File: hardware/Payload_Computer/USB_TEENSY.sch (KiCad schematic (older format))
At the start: 7 parts, among them J2 USB_B_Micro

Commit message: More Library Updates
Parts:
- J2: symbol Payload_Computer-rescue:USB_B_Micro-Symbols -> Symbols:USB_B_Micro
- U?: symbol Payload_Computer-rescue:MKL02Z32VFG4-Symbols -> Symbols:MKL02Z32VFG4
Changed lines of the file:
@@
 $EndDescr
 $Comp
-L Payload_Computer-rescue:USB_B_Micro-Symbols J2
+L Symbols:USB_B_Micro J2
 U 1 1 5F87457D
 P 3150 3500
@@
 ID
 $Comp
-L Payload_Computer-rescue:MKL02Z32VFG4-Symbols U?
+L Symbols:MKL02Z32VFG4 U?
 U 1 1 5FB00371
 P 8350 3200

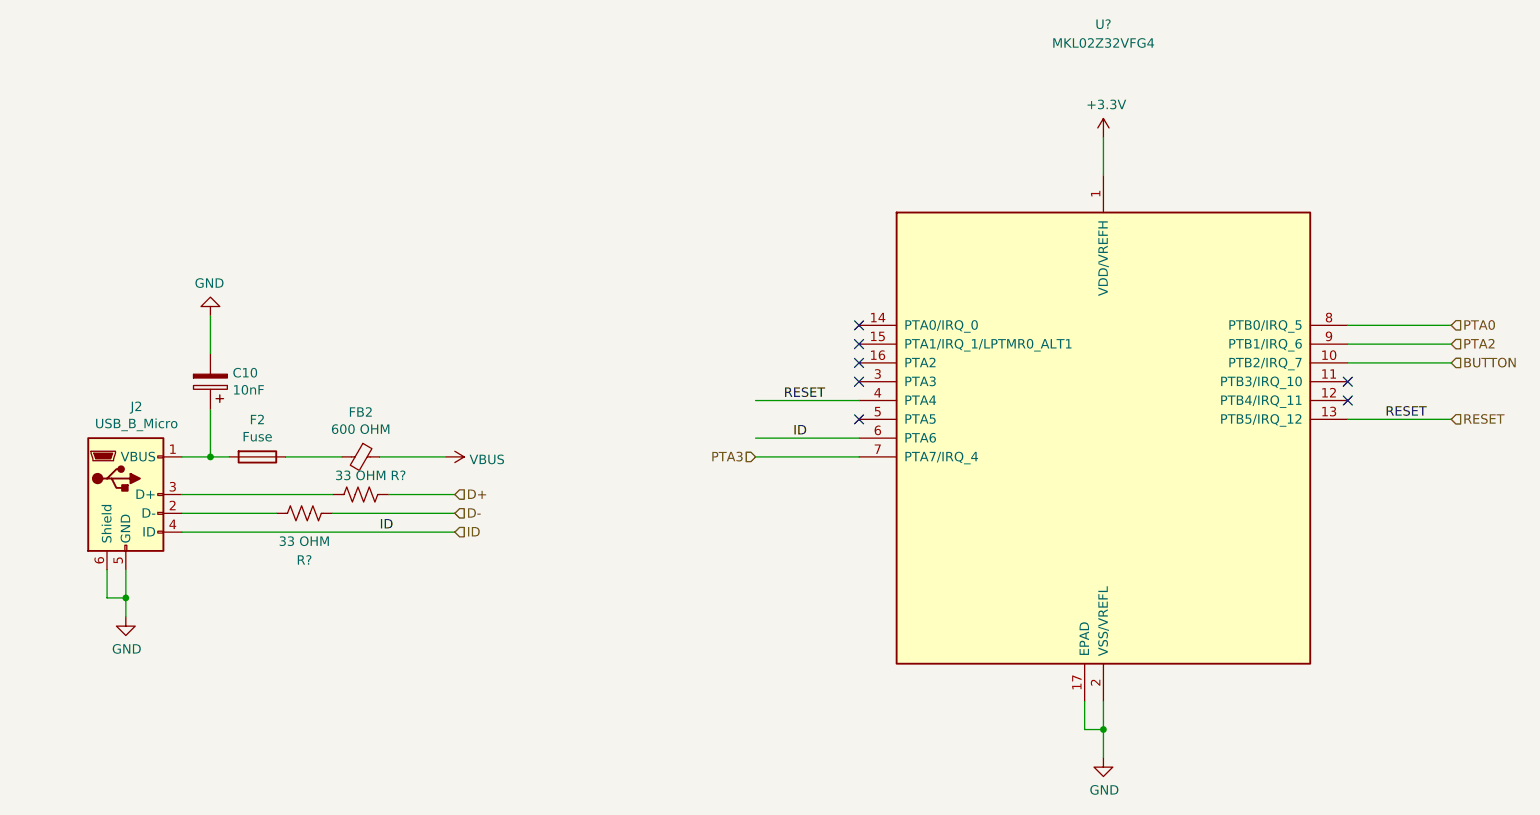
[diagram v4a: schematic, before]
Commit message: Finished Fan Schematic. Working on Servos
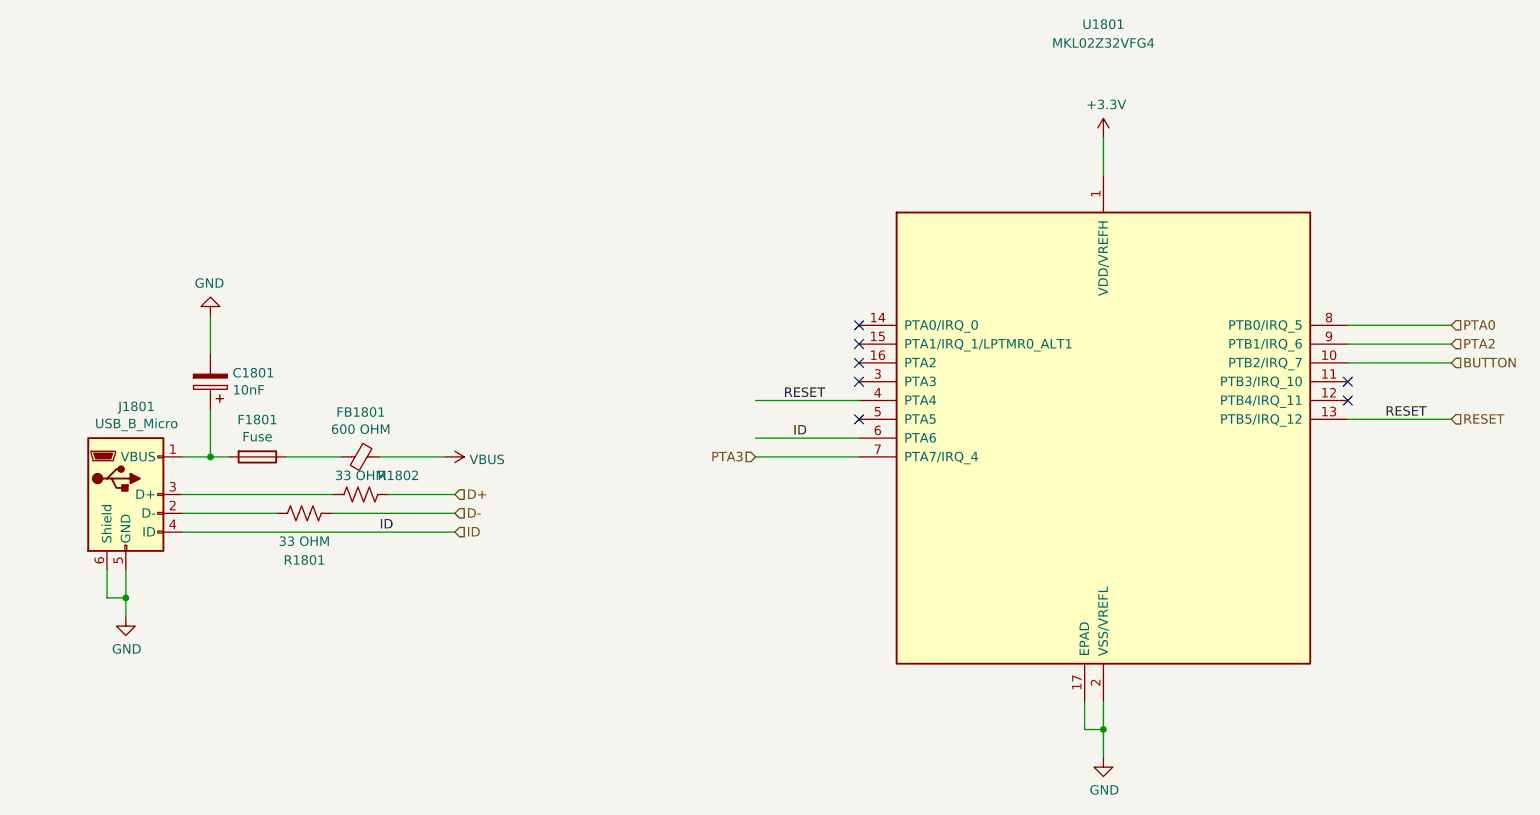
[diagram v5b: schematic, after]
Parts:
- C10: footprint (none) -> Capacitor_SMD:C_0603_1608Metric_Pad1.08x0.95mm_HandSolder
- R801, R802: renamed from R?; footprint (none) -> Resistor_SMD:R_0603_1608Metric_Pad0.98x0.95mm_HandSolder
- gave numbers to parts that had none: 1
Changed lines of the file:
@@
 $Descr A4 11693 8268
 encoding utf-8
-Sheet 8 26
+Sheet 18 22
 Title ""
 Date ""
@@
 P 3150 3500
 AR Path="/5F86D5A7/5F87457D" Ref="J2"  Part="1"
-AR Path="/60289E3E/5F87457D" Ref="J?"  Part="1"
-F 0 "J2" H 3207 3967 50  0000 C CNN
+AR Path="/60289E3E/5F87457D" Ref="J1801"  Part="1"
+F 0 "J1801" H 3207 3967 50  0000 C CNN
 F 1 "USB_B_Micro" H 3207 3876 50  0000 C CNN
 F 2 "" H 3300 3450 50  0001 C CNN
@@
 P 3850 3300
 AR Path="/5F86D5A7/5F874583" Ref="F2"  Part="1"
-AR Path="/60289E3E/5F874583" Ref="F?"  Part="1"
-F 0 "F2" V 3653 3300 50  0000 C CNN
+AR Path="/60289E3E/5F874583" Ref="F1801"  Part="1"
+F 0 "F1801" V 3653 3300 50  0000 C CNN
 F 1 "Fuse" V 3744 3300 50  0000 C CNN
 F 2 "" V 3780 3300 50  0001 C CNN
@@
 P 3600 2900
 AR Path="/5F86D5A7/5F87458A" Ref="C10"  Part="1"
-AR Path="/60289E3E/5F87458A" Ref="C?"  Part="1"
-F 0 "C10" H 3482 2854 50  0000 R CNN
+AR Path="/60289E3E/5F87458A" Ref="C1801"  Part="1"
+F 0 "C1801" H 3482 2854 50  0000 R CNN
 F 1 "10nF" H 3482 2945 50  0000 R CNN
-F 2 "" H 3638 2750 50  0001 C CNN
+F 2 "Capacitor_SMD:C_0603_1608Metric_Pad1.08x0.95mm_HandSolder" H 3638 2750 50  0001 C CNN
 F 3 "~" H 3600 2900 50  0001 C CNN
 	1    3600 2900
@@
 P 3600 2550
 AR Path="/5F86D5A7/5F874593" Ref="#PWR0117"  Part="1"
-AR Path="/60289E3E/5F874593" Ref="#PWR?"  Part="1"
-F 0 "#PWR0117" H 3600 2300 50  0001 C CNN
+AR Path="/60289E3E/5F874593" Ref="#PWR01802"  Part="1"
+F 0 "#PWR01802" H 3600 2300 50  0001 C CNN
 F 1 "GND" H 3605 2377 50  0000 C CNN
 F 2 "" H 3600 2550 50  0001 C CNN
@@
 P 4400 3300
 AR Path="/5F86D5A7/5F87459A" Ref="FB2"  Part="1"
-AR Path="/60289E3E/5F87459A" Ref="FB?"  Part="1"
-F 0 "FB2" V 4163 3300 50  0000 C CNN
+AR Path="/60289E3E/5F87459A" Ref="FB1801"  Part="1"
+F 0 "FB1801" V 4163 3300 50  0000 C CNN
 F 1 "600 OHM" V 4254 3300 50  0000 C CNN
 F 2 "" V 4330 3300 50  0001 C CNN
@@
 P 3150 4150
 AR Path="/5F86D5A7/5F8745A8" Ref="#PWR0119"  Part="1"
-AR Path="/60289E3E/5F8745A8" Ref="#PWR?"  Part="1"
-F 0 "#PWR0119" H 3150 3900 50  0001 C CNN
+AR Path="/60289E3E/5F8745A8" Ref="#PWR01801"  Part="1"
+F 0 "#PWR01801" H 3150 3900 50  0001 C CNN
 F 1 "GND" H 3155 3977 50  0000 C CNN
 F 2 "" H 3150 4150 50  0001 C CNN
@@
 	3450 3600 3950 3600
 $Comp
-L Device:R_US R?
+L Device:R_US R801
 U 1 1 5FAFD9D4
 P 4100 3600
-AR Path="/5F86D5A7/5FAFD9D4" Ref="R?"  Part="1"
-AR Path="/60289E3E/5FAFD9D4" Ref="R?"  Part="1"
-F 0 "R?" V 4350 3600 50  0000 C CNN
+AR Path="/5F86D5A7/5FAFD9D4" Ref="R801"  Part="1"
+AR Path="/60289E3E/5FAFD9D4" Ref="R1801"  Part="1"
+F 0 "R1801" V 4350 3600 50  0000 C CNN
 F 1 "33 OHM" V 4250 3600 50  0000 C CNN
-F 2 "" V 4140 3590 50  0001 C CNN
+F 2 "Resistor_SMD:R_0603_1608Metric_Pad0.98x0.95mm_HandSolder" V 4140 3590 50  0001 C CNN
 F 3 "~" H 4100 3600 50  0001 C CNN
 	1    4100 3600
@@
 $EndComp
 $Comp
-L Device:R_US R?
+L Device:R_US R802
 U 1 1 5FAFE37D
 P 4400 3500
-AR Path="/5F86D5A7/5FAFE37D" Ref="R?"  Part="1"
-AR Path="/60289E3E/5FAFE37D" Ref="R?"  Part="1"
-F 0 "R?" V 4300 3700 50  0000 C CNN
+AR Path="/5F86D5A7/5FAFE37D" Ref="R802"  Part="1"
+AR Path="/60289E3E/5FAFE37D" Ref="R1802"  Part="1"
+F 0 "R1802" V 4300 3700 50  0000 C CNN
 F 1 "33 OHM" V 4300 3500 50  0000 C CNN
-F 2 "" V 4440 3490 50  0001 C CNN
+F 2 "Resistor_SMD:R_0603_1608Metric_Pad0.98x0.95mm_HandSolder" V 4440 3490 50  0001 C CNN
 F 3 "~" H 4400 3500 50  0001 C CNN
 	1    4400 3500
@@
 ID
 $Comp
-L Symbols:MKL02Z32VFG4 U?
+L Symbols:MKL02Z32VFG4 U801
 U 1 1 5FB00371
 P 8350 3200
-AR Path="/5F86D5A7/5FB00371" Ref="U?"  Part="1"
-AR Path="/60289E3E/5FB00371" Ref="U?"  Part="1"
-F 0 "U?" H 8350 5400 50  0000 C CNN
+AR Path="/5F86D5A7/5FB00371" Ref="U801"  Part="1"
+AR Path="/60289E3E/5FB00371" Ref="U1801"  Part="1"
+F 0 "U1801" H 8350 5400 50  0000 C CNN
 F 1 "MKL02Z32VFG4" H 8350 5300 50  0000 C CNN
 F 2 "Package_DFN_QFN:QFN-16-1EP_3x3mm_P0.5mm_EP1.9x1.9mm" H 8500 1975 50  0001 L TNN
@@
 $EndComp
 $Comp
-L power:+3.3V #PWR?
+L power:+3.3V #PWR0802
 U 1 1 5FB010A8
 P 8350 1600
-AR Path="/5F86D5A7/5FB010A8" Ref="#PWR?"  Part="1"
-AR Path="/60289E3E/5FB010A8" Ref="#PWR?"  Part="1"
-F 0 "#PWR?" H 8350 1450 50  0001 C CNN
+AR Path="/5F86D5A7/5FB010A8" Ref="#PWR0802"  Part="1"
+AR Path="/60289E3E/5FB010A8" Ref="#PWR01804"  Part="1"
+F 0 "#PWR01804" H 8350 1450 50  0001 C CNN
 F 1 "+3.3V" H 8365 1773 50  0000 C CNN
 F 2 "" H 8350 1600 50  0001 C CNN
@@
 NoConn ~ 7050 2800
 $Comp
-L power:GND #PWR?
+L power:GND #PWR0803
 U 1 1 5FB025B3
 P 8350 4900
-AR Path="/5F86D5A7/5FB025B3" Ref="#PWR?"  Part="1"
-AR Path="/60289E3E/5FB025B3" Ref="#PWR?"  Part="1"
-F 0 "#PWR?" H 8350 4650 50  0001 C CNN
+AR Path="/5F86D5A7/5FB025B3" Ref="#PWR0803"  Part="1"
+AR Path="/60289E3E/5FB025B3" Ref="#PWR01805"  Part="1"
+F 0 "#PWR01805" H 8350 4650 50  0001 C CNN
 F 1 "GND" H 8355 4727 50  0000 C CNN
 F 2 "" H 8350 4900 50  0001 C CNN
@@
 	9650 2700 10200 2700
 $Comp
-L power:VBUS #PWR?
+L power:VBUS #PWR0801
 U 1 1 5FC29DFB
 P 4850 3300
-AR Path="/5F86D5A7/5FC29DFB" Ref="#PWR?"  Part="1"
-AR Path="/60289E3E/5FC29DFB" Ref="#PWR?"  Part="1"
-F 0 "#PWR?" H 4850 3150 50  0001 C CNN
+AR Path="/5F86D5A7/5FC29DFB" Ref="#PWR0801"  Part="1"
+AR Path="/60289E3E/5FC29DFB" Ref="#PWR01803"  Part="1"
+F 0 "#PWR01803" H 4850 3150 50  0001 C CNN
 F 1 "VBUS" V 4865 3428 50  0000 L CNN
 F 2 "" H 4850 3300 50  0001 C CNN

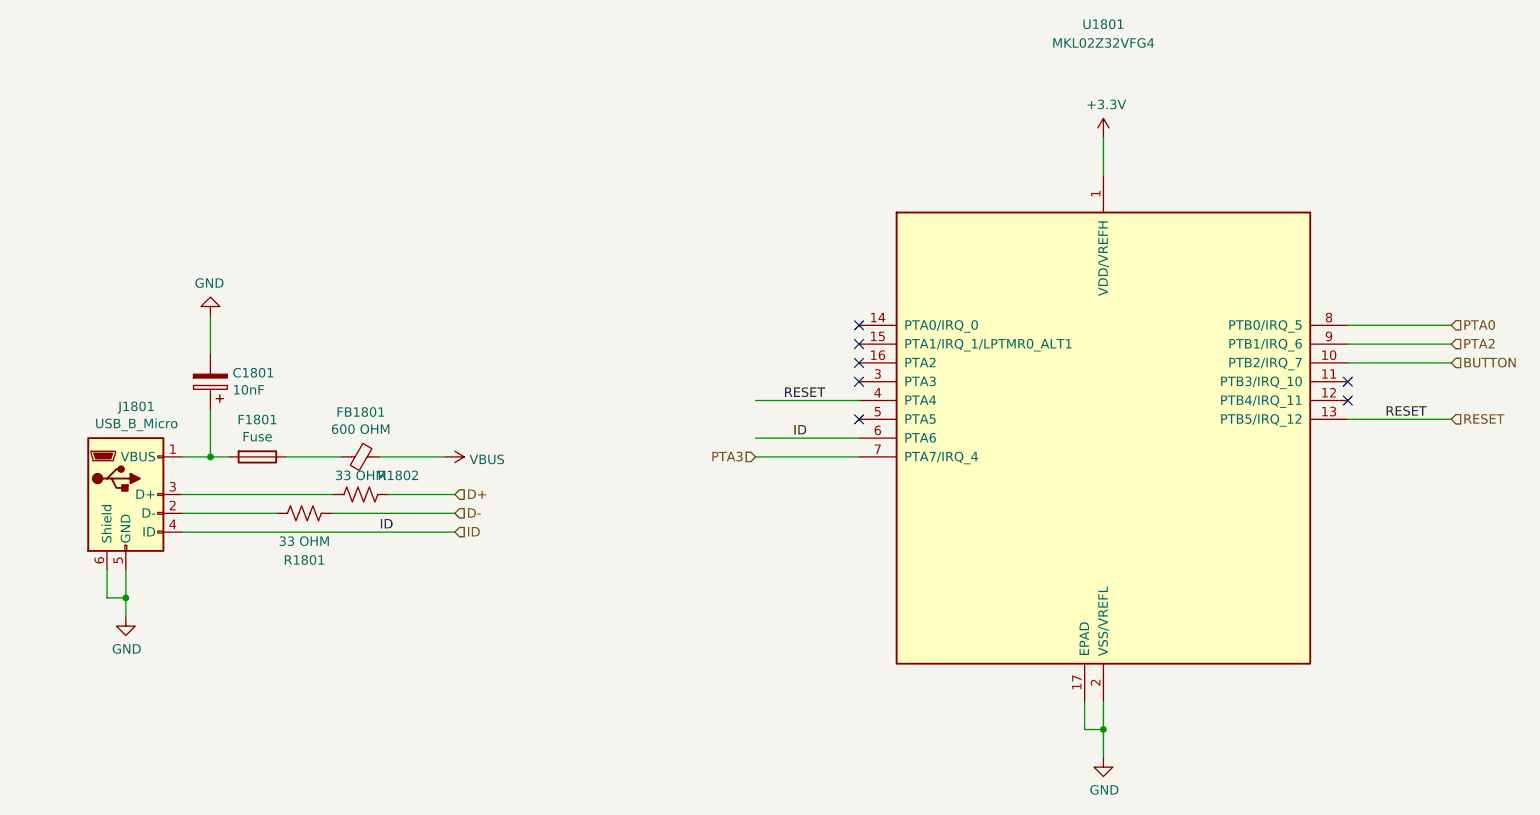
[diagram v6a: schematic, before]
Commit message: Added some footprints
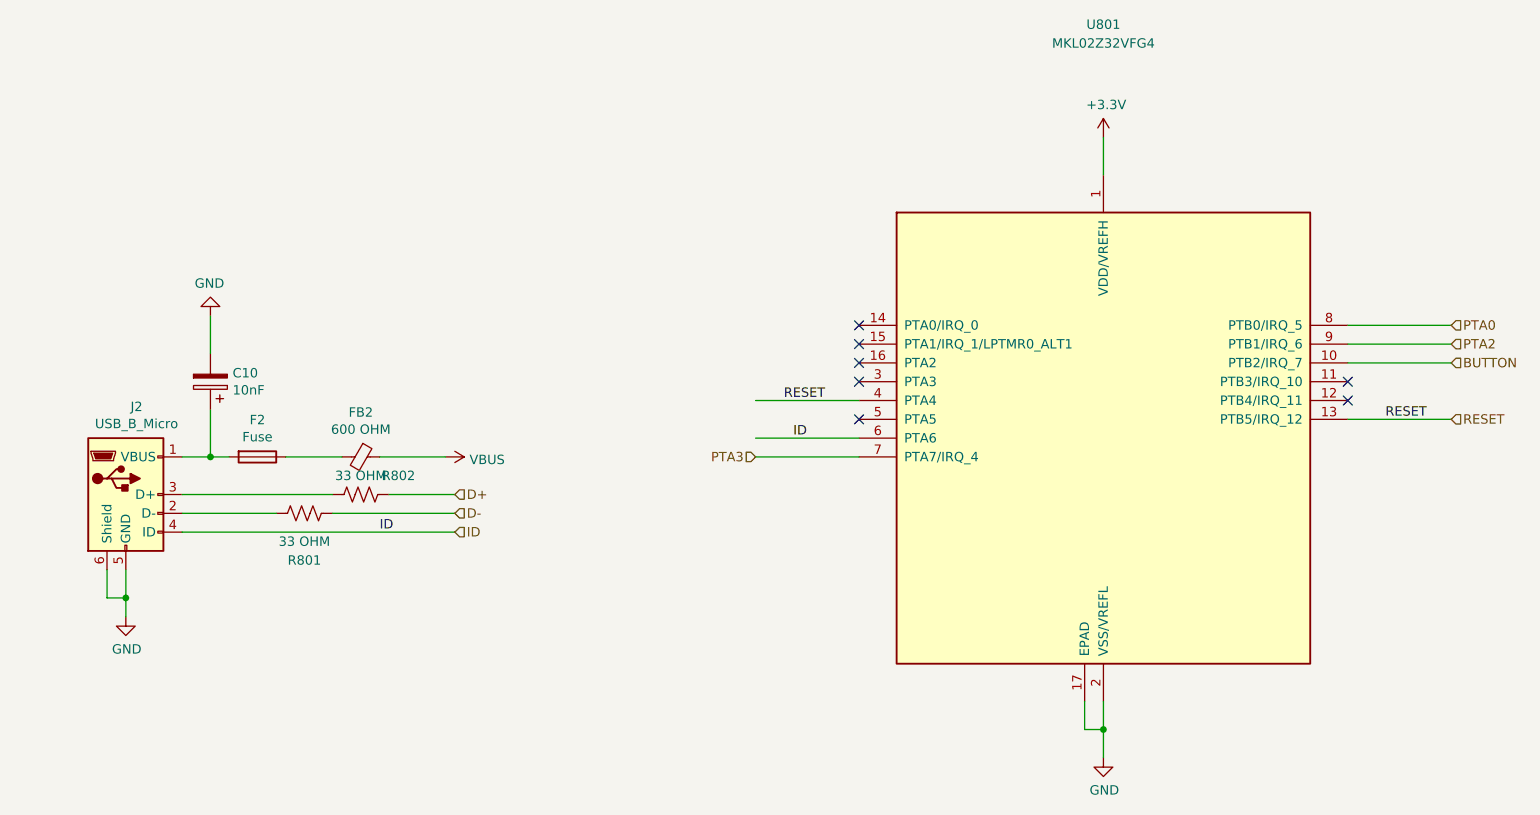
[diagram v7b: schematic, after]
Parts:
- FB2: footprint (none) -> Capacitor_SMD:C_0603_1608Metric_Pad1.08x0.95mm_HandSolder
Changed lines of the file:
@@
 $Descr A4 11693 8268
 encoding utf-8
-Sheet 12 18
+Sheet 8 18
 Title ""
 Date ""
@@
 AR Path="/5F86D5A7/5F87457D" Ref="J2"  Part="1"
 AR Path="/60289E3E/5F87457D" Ref="J1801"  Part="1"
-F 0 "J1801" H 3207 3967 50  0000 C CNN
+F 0 "J2" H 3207 3967 50  0000 C CNN
 F 1 "USB_B_Micro" H 3207 3876 50  0000 C CNN
 F 2 "" H 3300 3450 50  0001 C CNN
@@
 AR Path="/5F86D5A7/5F874583" Ref="F2"  Part="1"
 AR Path="/60289E3E/5F874583" Ref="F1801"  Part="1"
-F 0 "F1801" V 3653 3300 50  0000 C CNN
+F 0 "F2" V 3653 3300 50  0000 C CNN
 F 1 "Fuse" V 3744 3300 50  0000 C CNN
 F 2 "" V 3780 3300 50  0001 C CNN
@@
 AR Path="/5F86D5A7/5F87458A" Ref="C10"  Part="1"
 AR Path="/60289E3E/5F87458A" Ref="C1801"  Part="1"
-F 0 "C1801" H 3482 2854 50  0000 R CNN
+F 0 "C10" H 3482 2854 50  0000 R CNN
 F 1 "10nF" H 3482 2945 50  0000 R CNN
 F 2 "Capacitor_SMD:C_0603_1608Metric_Pad1.08x0.95mm_HandSolder" H 3638 2750 50  0001 C CNN
@@
 AR Path="/5F86D5A7/5F874593" Ref="#PWR0117"  Part="1"
 AR Path="/60289E3E/5F874593" Ref="#PWR01802"  Part="1"
-F 0 "#PWR01802" H 3600 2300 50  0001 C CNN
+F 0 "#PWR0117" H 3600 2300 50  0001 C CNN
 F 1 "GND" H 3605 2377 50  0000 C CNN
 F 2 "" H 3600 2550 50  0001 C CNN
@@
 AR Path="/5F86D5A7/5F87459A" Ref="FB2"  Part="1"
 AR Path="/60289E3E/5F87459A" Ref="FB1801"  Part="1"
-F 0 "FB1801" V 4163 3300 50  0000 C CNN
+F 0 "FB2" V 4163 3300 50  0000 C CNN
 F 1 "600 OHM" V 4254 3300 50  0000 C CNN
-F 2 "" V 4330 3300 50  0001 C CNN
+F 2 "Capacitor_SMD:C_0603_1608Metric_Pad1.08x0.95mm_HandSolder" V 4330 3300 50  0001 C CNN
 F 3 "~" H 4400 3300 50  0001 C CNN
 	1    4400 3300
@@
 AR Path="/5F86D5A7/5F8745A8" Ref="#PWR0119"  Part="1"
 AR Path="/60289E3E/5F8745A8" Ref="#PWR01801"  Part="1"
-F 0 "#PWR01801" H 3150 3900 50  0001 C CNN
+F 0 "#PWR0119" H 3150 3900 50  0001 C CNN
 F 1 "GND" H 3155 3977 50  0000 C CNN
 F 2 "" H 3150 4150 50  0001 C CNN
@@
 AR Path="/5F86D5A7/5FAFD9D4" Ref="R801"  Part="1"
 AR Path="/60289E3E/5FAFD9D4" Ref="R1801"  Part="1"
-F 0 "R1801" V 4350 3600 50  0000 C CNN
+F 0 "R801" V 4350 3600 50  0000 C CNN
 F 1 "33 OHM" V 4250 3600 50  0000 C CNN
 F 2 "Resistor_SMD:R_0603_1608Metric_Pad0.98x0.95mm_HandSolder" V 4140 3590 50  0001 C CNN
@@
 AR Path="/5F86D5A7/5FAFE37D" Ref="R802"  Part="1"
 AR Path="/60289E3E/5FAFE37D" Ref="R1802"  Part="1"
-F 0 "R1802" V 4300 3700 50  0000 C CNN
+F 0 "R802" V 4300 3700 50  0000 C CNN
 F 1 "33 OHM" V 4300 3500 50  0000 C CNN
 F 2 "Resistor_SMD:R_0603_1608Metric_Pad0.98x0.95mm_HandSolder" V 4440 3490 50  0001 C CNN
@@
 AR Path="/5F86D5A7/5FB00371" Ref="U801"  Part="1"
 AR Path="/60289E3E/5FB00371" Ref="U1801"  Part="1"
-F 0 "U1801" H 8350 5400 50  0000 C CNN
+F 0 "U801" H 8350 5400 50  0000 C CNN
 F 1 "MKL02Z32VFG4" H 8350 5300 50  0000 C CNN
 F 2 "Package_DFN_QFN:QFN-16-1EP_3x3mm_P0.5mm_EP1.9x1.9mm" H 8500 1975 50  0001 L TNN
@@
 AR Path="/5F86D5A7/5FB010A8" Ref="#PWR0802"  Part="1"
 AR Path="/60289E3E/5FB010A8" Ref="#PWR01804"  Part="1"
-F 0 "#PWR01804" H 8350 1450 50  0001 C CNN
+F 0 "#PWR0802" H 8350 1450 50  0001 C CNN
 F 1 "+3.3V" H 8365 1773 50  0000 C CNN
 F 2 "" H 8350 1600 50  0001 C CNN
@@
 AR Path="/5F86D5A7/5FB025B3" Ref="#PWR0803"  Part="1"
 AR Path="/60289E3E/5FB025B3" Ref="#PWR01805"  Part="1"
-F 0 "#PWR01805" H 8350 4650 50  0001 C CNN
+F 0 "#PWR0803" H 8350 4650 50  0001 C CNN
 F 1 "GND" H 8355 4727 50  0000 C CNN
 F 2 "" H 8350 4900 50  0001 C CNN
@@
 AR Path="/5F86D5A7/5FC29DFB" Ref="#PWR0801"  Part="1"
 AR Path="/60289E3E/5FC29DFB" Ref="#PWR01803"  Part="1"
-F 0 "#PWR01803" H 4850 3150 50  0001 C CNN
+F 0 "#PWR0801" H 4850 3150 50  0001 C CNN
 F 1 "VBUS" V 4865 3428 50  0000 L CNN
 F 2 "" H 4850 3300 50  0001 C CNN

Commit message: Added footprints to fuse and led
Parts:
- F2: footprint (none) -> Fuse:Fuse_0603_1608Metric_Pad1.05x0.95mm_HandSolder
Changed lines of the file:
@@
 F 0 "F2" V 3653 3300 50  0000 C CNN
 F 1 "Fuse" V 3744 3300 50  0000 C CNN
-F 2 "" V 3780 3300 50  0001 C CNN
+F 2 "Fuse:Fuse_0603_1608Metric_Pad1.05x0.95mm_HandSolder" V 3780 3300 50  0001 C CNN
 F 3 "~" H 3850 3300 50  0001 C CNN
 	1    3850 3300
